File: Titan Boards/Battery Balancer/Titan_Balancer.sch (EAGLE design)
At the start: 84 parts, among them IC1 REG1117, IC2 SN74LV11AD, IC3 SN74LS04N, P1 39-30-04, P2 39-30-10, P4 39-30-04, P5 39-30-06, Q1 SPD30P06PTO252, Q12 310mA/60V/1.6Ω, Q2 SPB80P06P, Q3 SPB80P06P, Q4 SPD30P06PTO252, Q5 MOSFET-NCH-AO3404A, Q9 MOSFET-NCH-AO3404A, U1 I6A4W020A033V-001-R, U2 I6A4W020A033V-001-R

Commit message: worked a bit on board and fixed schematic error on sheet 3
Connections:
- removed net N$6: R1.1, R1.2, R2.1, R4.1, U$9.A1
- new net N$33: R1.2, R2.1, U$9.A1
- net +3V3: now also R1.1, R4.1
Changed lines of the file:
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@@
 <?xml version="1.0" encoding="utf-8"?>
 <!DOCTYPE eagle SYSTEM "eagle.dtd">
-<eagle version="9.5.2">
+<eagle version="9.6.2">
 <drawing>
 <settings>
@@
 <pinref part="U$9" gate="G$1" pin="V+"/>
 <pinref part="+3V3" gate="G$1" pin="+3V3"/>
-<wire x1="43.18" y1="38.1" x2="43.18" y2="33.02" width="0.1524" layer="91"/>
+<wire x1="43.18" y1="38.1" x2="43.18" y2="35.56" width="0.1524" layer="91"/>
+<wire x1="43.18" y1="35.56" x2="43.18" y2="33.02" width="0.1524" layer="91"/>
+<wire x1="10.16" y1="35.56" x2="43.18" y2="35.56" width="0.1524" layer="91"/>
+<wire x1="10.16" y1="35.56" x2="10.16" y2="30.48" width="0.1524" layer="91"/>
+<pinref part="R1" gate="G$1" pin="1"/>
+<wire x1="10.16" y1="30.48" x2="10.16" y2="20.32" width="0.1524" layer="91"/>
+<wire x1="10.16" y1="20.32" x2="12.7" y2="20.32" width="0.1524" layer="91"/>
+<pinref part="R4" gate="G$1" pin="1"/>
+<wire x1="10.16" y1="30.48" x2="12.7" y2="30.48" width="0.1524" layer="91"/>
+<junction x="10.16" y="30.48"/>
+<junction x="43.18" y="35.56"/>
 </segment>
 </net>
@@
 </segment>
 </net>
-<net name="N$6" class="0">
-<segment>
-<wire x1="27.94" y1="12.7" x2="25.4" y2="12.7" width="0.1524" layer="91"/>
-<wire x1="25.4" y1="12.7" x2="25.4" y2="20.32" width="0.1524" layer="91"/>
-<wire x1="25.4" y1="20.32" x2="25.4" y2="35.56" width="0.1524" layer="91"/>
-<wire x1="25.4" y1="35.56" x2="27.94" y2="35.56" width="0.1524" layer="91"/>
-<pinref part="U$9" gate="G$1" pin="A1"/>
-<wire x1="27.94" y1="35.56" x2="27.94" y2="38.1" width="0.1524" layer="91"/>
-<wire x1="25.4" y1="20.32" x2="22.86" y2="20.32" width="0.1524" layer="91"/>
-<junction x="25.4" y="20.32"/>
-<wire x1="10.16" y1="35.56" x2="25.4" y2="35.56" width="0.1524" layer="91"/>
-<junction x="25.4" y="35.56"/>
-<pinref part="R2" gate="G$1" pin="1"/>
-<pinref part="R1" gate="G$1" pin="2"/>
-<wire x1="10.16" y1="35.56" x2="10.16" y2="30.48" width="0.1524" layer="91"/>
-<pinref part="R1" gate="G$1" pin="1"/>
-<wire x1="10.16" y1="30.48" x2="10.16" y2="20.32" width="0.1524" layer="91"/>
-<wire x1="10.16" y1="20.32" x2="12.7" y2="20.32" width="0.1524" layer="91"/>
-<pinref part="R4" gate="G$1" pin="1"/>
-<wire x1="10.16" y1="30.48" x2="12.7" y2="30.48" width="0.1524" layer="91"/>
-<junction x="10.16" y="30.48"/>
-</segment>
-</net>
 <net name="N$7" class="0">
 <segment>
@@
 </segment>
 </net>
+<net name="N$33" class="0">
+<segment>
+<pinref part="R1" gate="G$1" pin="2"/>
+<wire x1="25.4" y1="20.32" x2="22.86" y2="20.32" width="0.1524" layer="91"/>
+<pinref part="R2" gate="G$1" pin="1"/>
+<wire x1="27.94" y1="12.7" x2="25.4" y2="12.7" width="0.1524" layer="91"/>
+<wire x1="25.4" y1="12.7" x2="25.4" y2="20.32" width="0.1524" layer="91"/>
+<pinref part="U$9" gate="G$1" pin="A1"/>
+<wire x1="27.94" y1="38.1" x2="27.94" y2="20.32" width="0.1524" layer="91"/>
+<wire x1="27.94" y1="20.32" x2="25.4" y2="20.32" width="0.1524" layer="91"/>
+<junction x="25.4" y="20.32"/>
+</segment>
+</net>

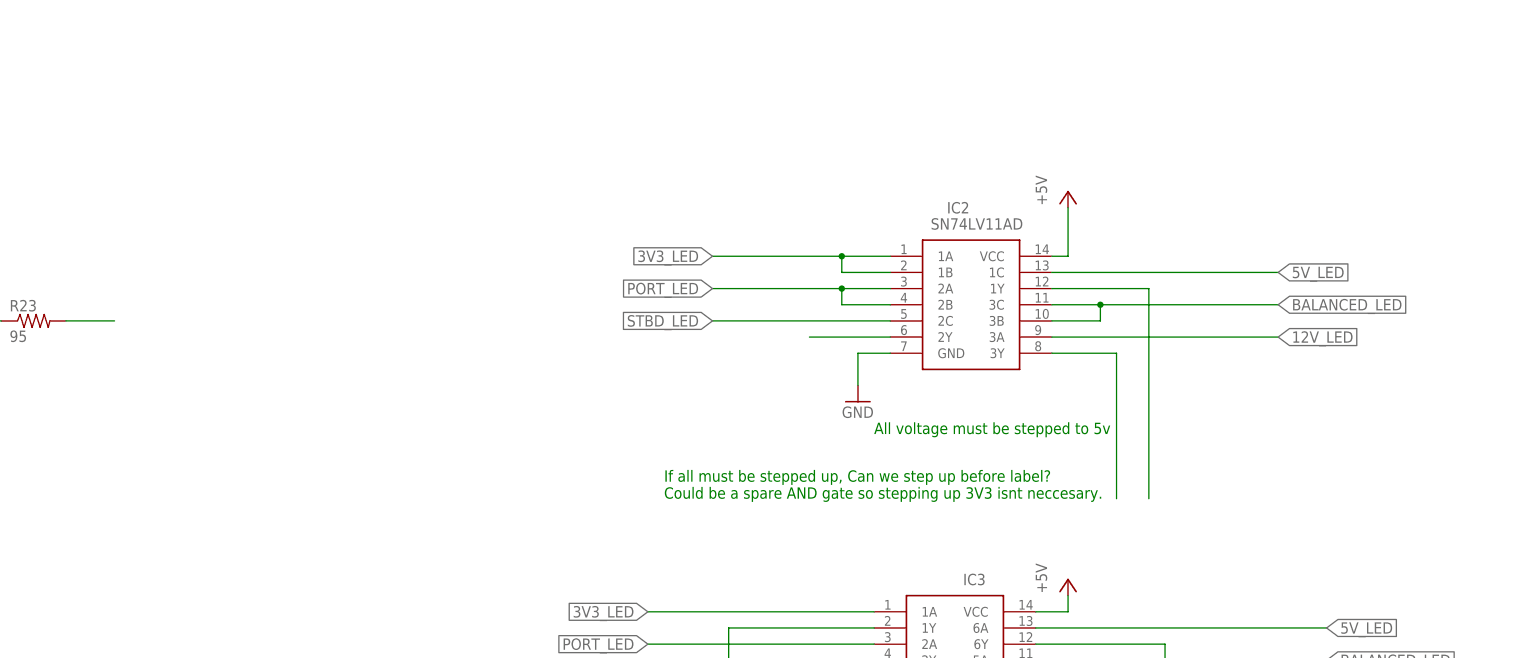
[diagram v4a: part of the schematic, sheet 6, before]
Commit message: Stepped up for AND
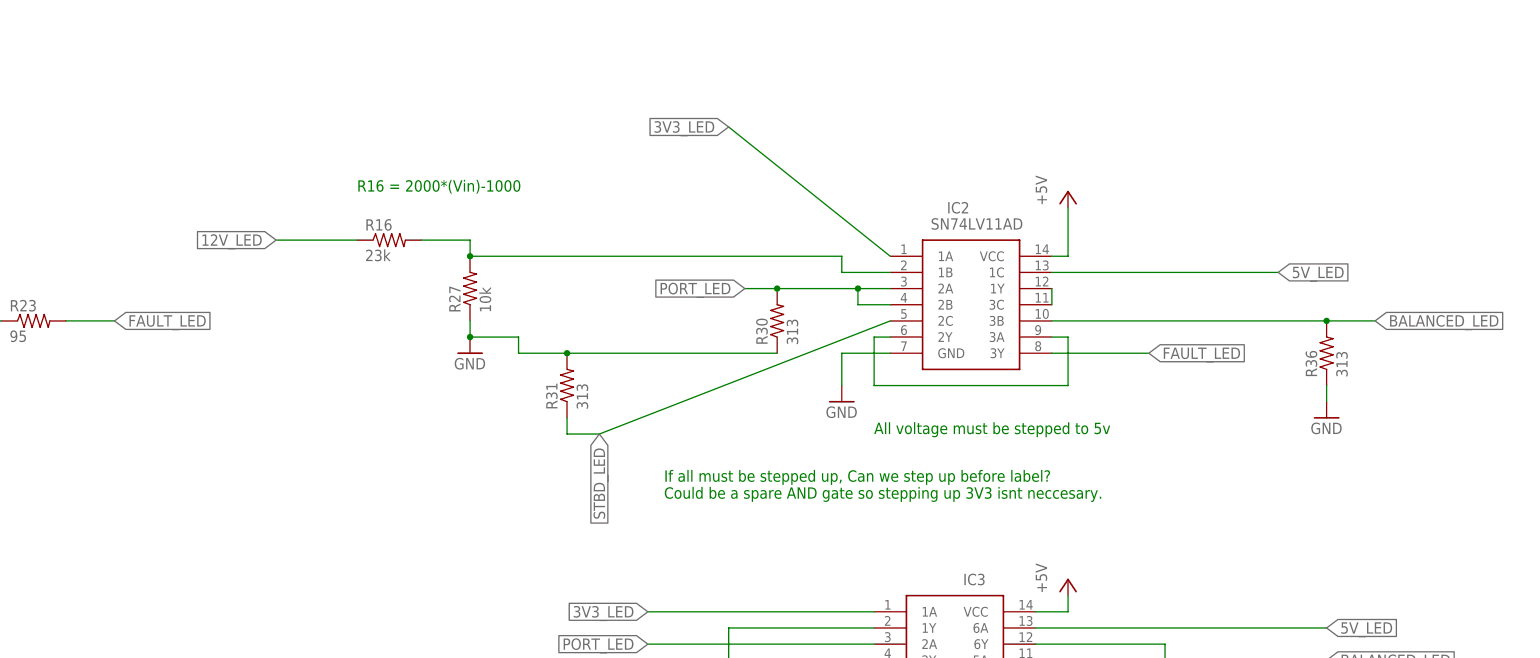
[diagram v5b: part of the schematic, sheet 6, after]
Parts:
- removed R17: 470, rcl:R-US_R0603
- added R27: 10k, rcl:R-US_R0603
- added R30, R31, R36: 313, rcl:R-US_R0603
- R16: value 470 -> 23k
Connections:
- removed net N$26: IC2.3Y
- removed net N$27: IC2.2Y
- new net FAULT_LED: IC2.3Y, R23.2
- new net N$6: IC2.1Y, IC2.3C
- net +12V: no longer C5.1, C7.1, C8.1, R16.2, U2.SENSE+, U2.VOUT(+)
- net +5V: no longer C10.1, C11.1, C9.1, R17.2, U1.SENSE+, U1.VOUT(+)
- net 12V_LED: now also C5.1, C7.1, C8.1, U2.SENSE+, U2.VOUT(+); no longer IC2.3A
- net 3V3_LED: no longer IC2.1B
- net 5V_LED: now also C10.1, C11.1, C9.1, U1.SENSE+, U1.VOUT(+); no longer R17.1
- net BALANCED_LED: now also R36.2; no longer IC2.3C
- net GND: now also R27.1, R30.1, R31.2, R36.1
- net N$1: now also IC2.1B, R16.2, R27.2; no longer R23.2
- net N$9: now also IC2.2Y, IC2.3A; no longer IC2.1Y
- net PORT_LED: now also R30.2
- net STBD_LED: now also R31.1
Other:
- note added: "R16 = 2000*(Vin)-1000"

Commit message: cleaned up sheet 6 of pd board
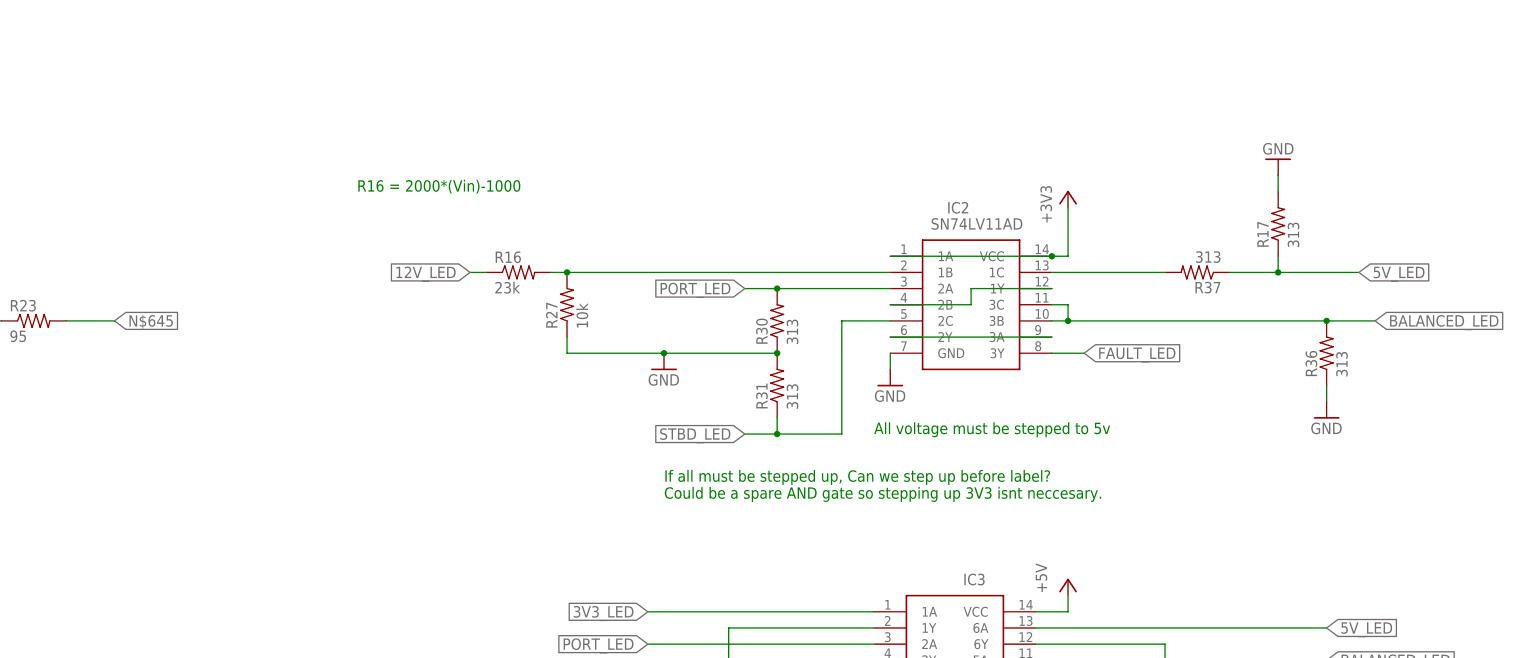
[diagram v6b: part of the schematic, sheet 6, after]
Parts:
- added R17, R37: 313, rcl:R-US_R0603
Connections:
- new net N$26: IC2.1C, R37.2
- new net N$645: R23.2
- net +3V3: now also IC2.1A, IC2.VCC
- net +5V: no longer IC2.VCC
- net 3V3_LED: no longer IC2.1A
- net 5V_LED: now also R17.1, R37.1; no longer IC2.1C
- net BALANCED_LED: now also IC2.3C
- net FAULT_LED: no longer R23.2
- net GND: now also R17.2
- net N$6: now also IC2.2B; no longer IC2.3C
- net PORT_LED: no longer IC2.2B
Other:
- moved on the sheet: R16, R27, R31

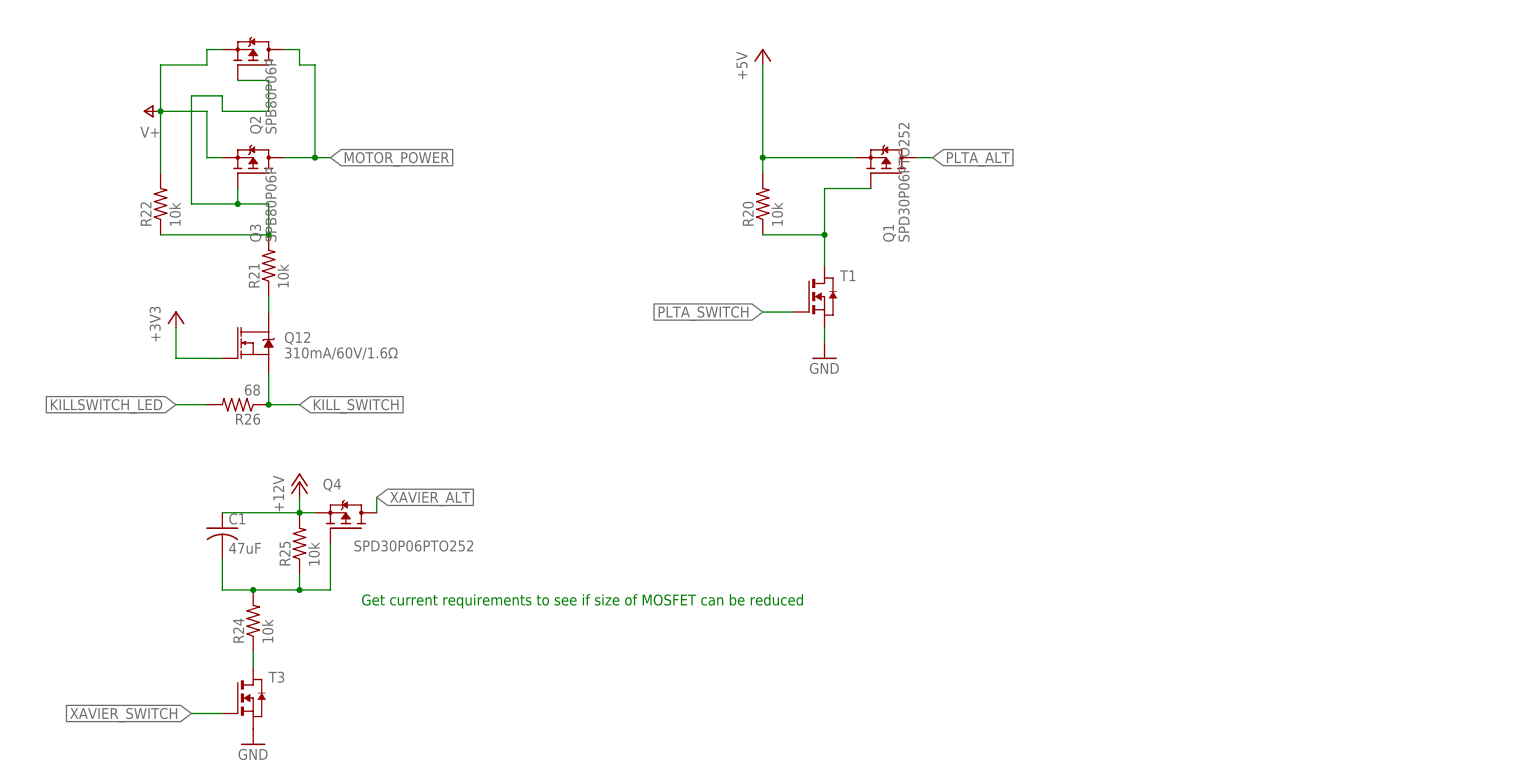
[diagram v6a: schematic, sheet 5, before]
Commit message: fixed mismatched inverter inputs and outputs, fixed (?) 5V LED
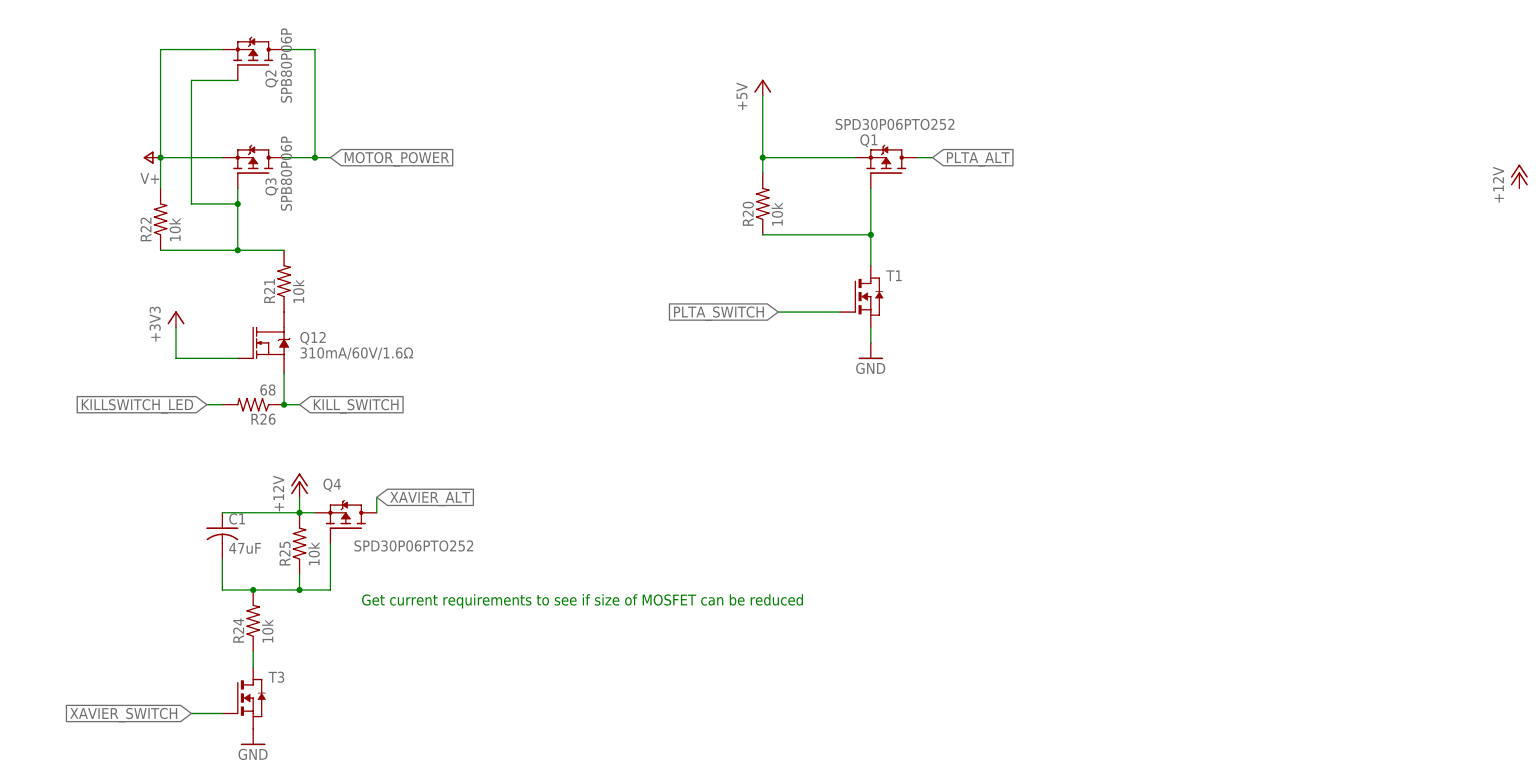
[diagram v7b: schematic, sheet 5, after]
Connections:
- removed net N$32: BALANCED.A, IC3.6Y
- net +5V: now also 5V.C
- net 5V_LED: no longer IC3.6A
- net GND: now also IC3.6A, IC3.6Y; no longer 5V.C
- net N$1: now also 5V.A
- net N$31: now also BALANCED.A; no longer 5V.A
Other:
- moved on the sheet: 5V, BALANCED, Q12, R11, R12, R21, R22, R26, T1

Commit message: organization part1
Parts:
- added R38: 313, rcl:R-US_R0603
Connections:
- removed net N$645: R23.2
- new net N$32: 12V.C, 3V3.C, BALANCED.C, PORT.C, R38.2, STBD.C
- net FAULT_LED: now also R23.2
- net GND: now also R38.1; no longer 12V.C, 3V3.C, BALANCED.C, PORT.C, STBD.C
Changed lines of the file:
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@@
 <?xml version="1.0" encoding="utf-8"?>
 <!DOCTYPE eagle SYSTEM "eagle.dtd">
-<eagle version="9.6.2">
+<eagle version="9.5.2">
 <drawing>
 <settings>
@@
 <part name="P+17" library="supply1" library_urn="urn:adsk.eagle:library:371" deviceset="+12V" device=""/>
 <part name="P+19" library="supply1" library_urn="urn:adsk.eagle:library:371" deviceset="+5V" device=""/>
+<part name="R38" library="rcl" library_urn="urn:adsk.eagle:library:334" deviceset="R-US_" device="R0603" package3d_urn="urn:adsk.eagle:package:23555/3" value="313"/>
 </parts>
 <sheets>
@@
 <attribute name="VALUE" x="41.656" y="41.529" size="1.778" layer="96"/>
 </instance>
-<instance part="P+17" gate="1" x="254" y="104.14" smashed="yes">
-<attribute name="VALUE" x="251.46" y="99.06" size="1.778" layer="96" rot="R90"/>
+<instance part="P+17" gate="1" x="119.38" y="55.88" smashed="yes">
+<attribute name="VALUE" x="116.84" y="50.8" size="1.778" layer="96" rot="R90"/>
 </instance>
 </instances>
@@
 <attribute name="VALUE" x="196.85" y="109.22" size="1.778" layer="96" align="center-left"/>
 </instance>
-<instance part="GND26" gate="1" x="203.2" y="81.28" smashed="yes">
-<attribute name="VALUE" x="200.66" y="78.74" size="1.778" layer="96"/>
+<instance part="GND26" gate="1" x="203.2" y="76.2" smashed="yes">
+<attribute name="VALUE" x="200.66" y="73.66" size="1.778" layer="96"/>
 </instance>
 <instance part="P+18" gate="1" x="220.98" y="134.62" smashed="yes">
@@
 <attribute name="VALUE" x="144.78" y="210.82" size="1.778" layer="96" rot="R270"/>
 </instance>
+<instance part="R38" gate="G$1" x="208.28" y="86.36" smashed="yes" rot="R90">
+<attribute name="NAME" x="206.7814" y="82.55" size="1.778" layer="95" rot="R90"/>
+<attribute name="VALUE" x="211.582" y="82.55" size="1.778" layer="96" rot="R90"/>
+</instance>
 </instances>
 <busses>
@@
 </segment>
 <segment>
-<pinref part="IC3" gate="G$1" pin="GND"/>
-<wire x1="190.5" y1="114.3" x2="190.5" y2="109.22" width="0.1524" layer="91"/>
-<wire x1="190.5" y1="109.22" x2="203.2" y2="109.22" width="0.1524" layer="91"/>
-<pinref part="GND26" gate="1" pin="GND"/>
-<wire x1="203.2" y1="83.82" x2="203.2" y2="91.44" width="0.1524" layer="91"/>
-<pinref part="12V" gate="G$1" pin="C"/>
-<wire x1="203.2" y1="91.44" x2="203.2" y2="109.22" width="0.1524" layer="91"/>
-<wire x1="210.82" y1="96.52" x2="210.82" y2="91.44" width="0.1524" layer="91"/>
-<wire x1="210.82" y1="91.44" x2="203.2" y2="91.44" width="0.1524" layer="91"/>
-<junction x="203.2" y="91.44"/>
-<junction x="210.82" y="91.44"/>
-<wire x1="223.52" y1="91.44" x2="210.82" y2="91.44" width="0.1524" layer="91"/>
-<wire x1="203.2" y1="91.44" x2="195.58" y2="91.44" width="0.1524" layer="91"/>
-<pinref part="STBD" gate="G$1" pin="C"/>
-<wire x1="195.58" y1="91.44" x2="195.58" y2="96.52" width="0.1524" layer="91"/>
-<wire x1="195.58" y1="91.44" x2="180.34" y2="91.44" width="0.1524" layer="91"/>
-<junction x="195.58" y="91.44"/>
-<pinref part="PORT" gate="G$1" pin="C"/>
-<wire x1="180.34" y1="91.44" x2="180.34" y2="96.52" width="0.1524" layer="91"/>
-<wire x1="180.34" y1="91.44" x2="167.64" y2="91.44" width="0.1524" layer="91"/>
-<junction x="180.34" y="91.44"/>
-<pinref part="3V3" gate="G$1" pin="C"/>
-<wire x1="167.64" y1="91.44" x2="167.64" y2="96.52" width="0.1524" layer="91"/>
-<pinref part="BALANCED" gate="G$1" pin="C"/>
-<wire x1="223.52" y1="96.52" x2="223.52" y2="91.44" width="0.1524" layer="91"/>
-</segment>
-<segment>
 <pinref part="GND27" gate="1" pin="GND"/>
 <pinref part="R30" gate="G$1" pin="1"/>
@@
 <junction x="220.98" y="127"/>
 </segment>
+<segment>
+<pinref part="IC3" gate="G$1" pin="GND"/>
+<wire x1="190.5" y1="114.3" x2="190.5" y2="109.22" width="0.1524" layer="91"/>
+<wire x1="190.5" y1="109.22" x2="203.2" y2="109.22" width="0.1524" layer="91"/>
+<pinref part="GND26" gate="1" pin="GND"/>
+<wire x1="203.2" y1="109.22" x2="203.2" y2="78.74" width="0.1524" layer="91"/>
+<pinref part="R38" gate="G$1" pin="1"/>
+<wire x1="208.28" y1="81.28" x2="208.28" y2="78.74" width="0.1524" layer="91"/>
+<wire x1="208.28" y1="78.74" x2="203.2" y2="78.74" width="0.1524" layer="91"/>
+<junction x="203.2" y="78.74"/>
+</segment>
 </net>
 <net name="STBD_LED" class="0">
@@
 </segment>
 </net>
-<net name="N$645" class="0">
-<segment>
-<wire x1="71.12" y1="175.26" x2="63.5" y2="175.26" width="0.1524" layer="91"/>
-<pinref part="R23" gate="G$1" pin="2"/>
-<label x="71.12" y="175.26" size="1.778" layer="95" xref="yes"/>
-</segment>
-</net>
 <net name="N$20" class="0">
 <segment>
@@
 <label x="223.52" y="170.18" size="1.778" layer="95" xref="yes"/>
 </segment>
+<segment>
+<wire x1="71.12" y1="175.26" x2="63.5" y2="175.26" width="0.1524" layer="91"/>
+<pinref part="R23" gate="G$1" pin="2"/>
+<label x="71.12" y="175.26" size="1.778" layer="95" xref="yes"/>
+</segment>
 </net>
 <net name="N$6" class="0">
@@
 </segment>
 </net>
+<net name="N$32" class="0">
+<segment>
+<pinref part="12V" gate="G$1" pin="C"/>
+<wire x1="210.82" y1="96.52" x2="210.82" y2="91.44" width="0.1524" layer="91"/>
+<junction x="210.82" y="91.44"/>
+<wire x1="223.52" y1="91.44" x2="210.82" y2="91.44" width="0.1524" layer="91"/>
+<wire x1="210.82" y1="91.44" x2="208.28" y2="91.44" width="0.1524" layer="91"/>
+<pinref part="STBD" gate="G$1" pin="C"/>
+<wire x1="208.28" y1="91.44" x2="195.58" y2="91.44" width="0.1524" layer="91"/>
+<wire x1="195.58" y1="91.44" x2="195.58" y2="96.52" width="0.1524" layer="91"/>
+<wire x1="195.58" y1="91.44" x2="180.34" y2="91.44" width="0.1524" layer="91"/>
+<junction x="195.58" y="91.44"/>
+<pinref part="PORT" gate="G$1" pin="C"/>
+<wire x1="180.34" y1="91.44" x2="180.34" y2="96.52" width="0.1524" layer="91"/>
+<wire x1="180.34" y1="91.44" x2="167.64" y2="91.44" width="0.1524" layer="91"/>
+<junction x="180.34" y="91.44"/>
+<pinref part="3V3" gate="G$1" pin="C"/>
+<wire x1="167.64" y1="91.44" x2="167.64" y2="96.52" width="0.1524" layer="91"/>
+<pinref part="BALANCED" gate="G$1" pin="C"/>
+<wire x1="223.52" y1="96.52" x2="223.52" y2="91.44" width="0.1524" layer="91"/>
+<pinref part="R38" gate="G$1" pin="2"/>
+<junction x="208.28" y="91.44"/>
+</segment>
+</net>
